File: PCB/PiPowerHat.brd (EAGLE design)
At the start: 65 x 56 mm, 48 parts, among them J3 Display, J4 FAN1, K1 PIN20X2, Q1 NX2301P, U1 EEPROM24, U2 INA219AIDCNRSOIC, U3 TSL2561T, U4 DS18B20, U5 DS1820SOIC, U6 74AC125

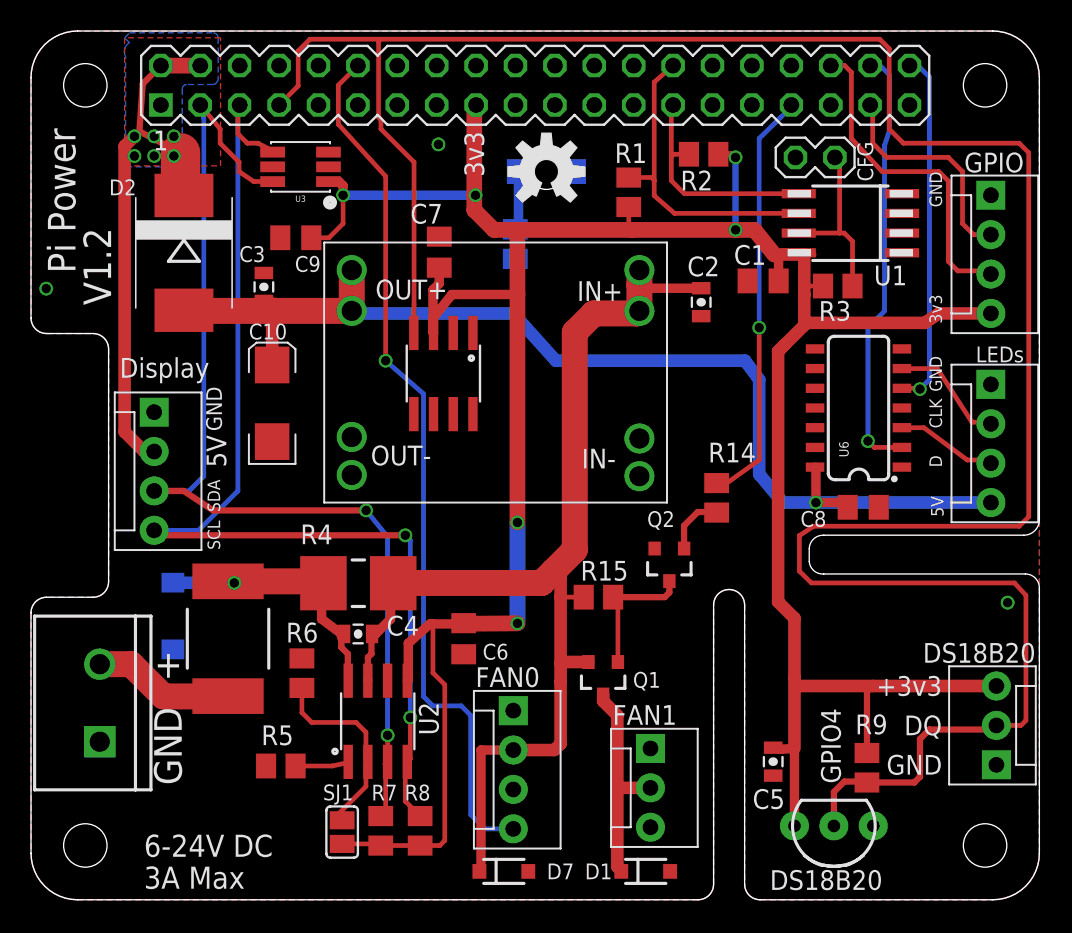
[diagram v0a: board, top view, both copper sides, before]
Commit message: Update to rearrange the board a bit better.
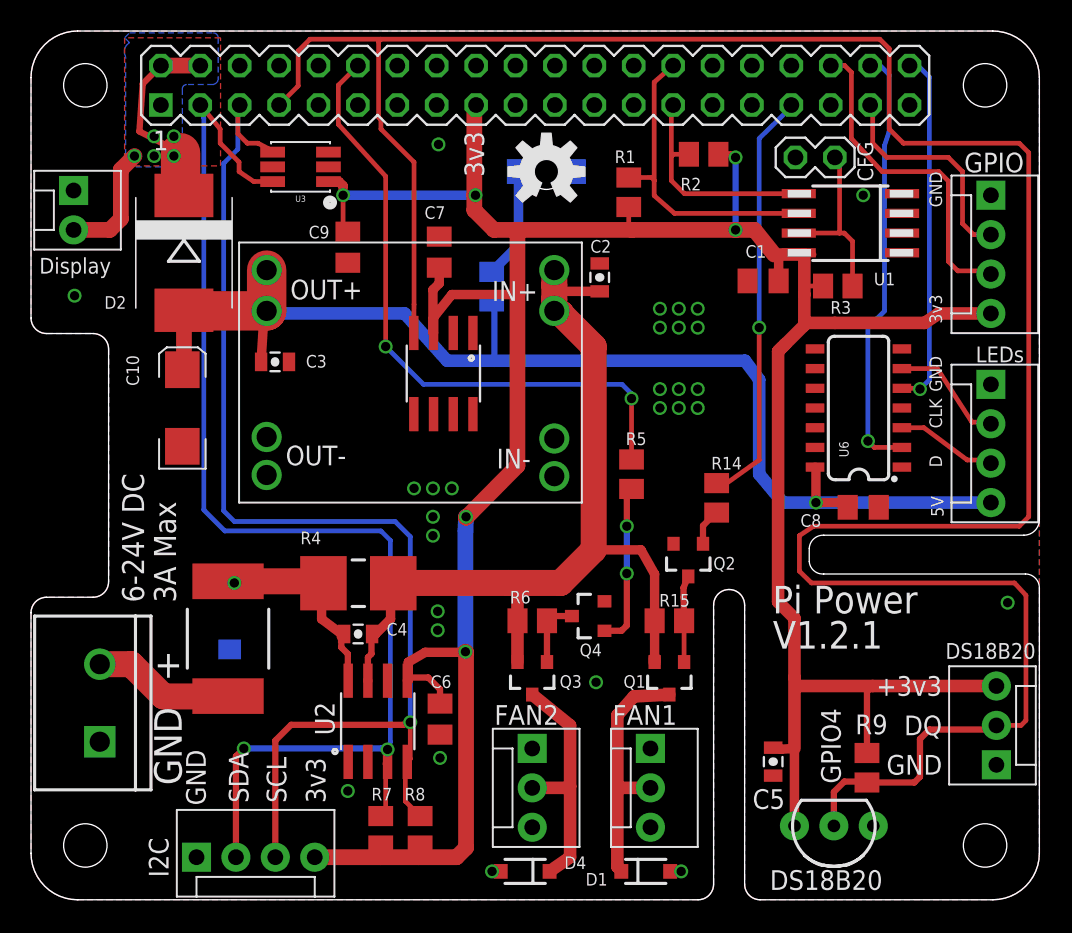
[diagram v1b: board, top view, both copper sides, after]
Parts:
- removed D7: (no value), SparkFun-DiscreteSemi:SOD-123
- removed JP2: FAN0, SparkFun-Connectors:MOLEX-1X4
- removed SJ1: (no value), jumper:SJ
- added D4: (no value), SparkFun-DiscreteSemi:SOD-123
- added J5: I2C, SparkFun-Connectors:MOLEX-1X4
- added JP3: Display, SparkFun-Connectors:MOLEX-1X2
- added Q3: NX2301P, SparkFun-DiscreteSemi:SOT23-3
- added Q4: (no value), SparkFun-DiscreteSemi:SOT23-3
- J3: value Display -> FAN2; device SparkFun-Connectors:MOLEX-1X4 -> SparkFun-Connectors:MOLEX-1X3
- moved J3 32.6 mm to (32.3, 9.75)
- moved R5 29.4 mm to (38.7, 27.4), turned to 90 degrees
- moved R6 15.2 mm to (32.3, 18.0), turned to 180 degrees
- moved C2 6.73 mm to (36.7, 40.1), turned to 270 degrees
- moved C10 5.80 mm to (9.75, 31.7)
- moved U$1 5.49 mm to (13.4, 25.6)
- moved C6 5.40 mm to (26.4, 11.6)
- moved C3 4.89 mm to (15.7, 34.7), turned to 180 degrees
- moved R15 4.82 mm to (41.1, 18.0)
- moved Q1 4.27 mm to (41.1, 14.3)
- moved D6 3.66 mm to (12.8, 18.3)
- moved C9 3.41 mm to (20.4, 42.1), turned to 270 degrees
- moved R12 3.14 mm to (29.7, 39.5)
- moved Q2 1.26 mm to (42.4, 21.9)
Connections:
- removed net FAN0_PWM: JP2.4, K1.12
- removed net N$10: R5.2, U2.1
- removed net N$9: R6.2, SJ1.2, U2.2
- new net FAN2_PWM: K1.12, R5.2
- new net GPIO6: K1.31
- new net N$1: D4.C, J3.2, Q3.3
- new net N$2: Q4.1, R5.1
- new net N$6: Q3.1, Q4.3, R6.1
- net +3V3: now also J5.4; no longer SJ1.1
- net GND: now also D4.A, J5.1, JP3.1, Q4.2, U2.1, U2.2; no longer D7.A, JP2.1, R5.1, R6.1
- net PI_5V: now also JP3.2; no longer J3.2
- net SCL: now also J5.3; no longer J3.4
- net SDA: now also J5.2; no longer J3.3
- net VIN: now also Q3.2, R6.2; no longer D7.C, JP2.2
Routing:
- net FAN0_PWM: track 56.5 -> 0.00 mm, vias 1 -> 0
- net FAN2_PWM: track 0.00 -> 41.2 mm, vias 0 -> 2
- net N$1: track 0.00 -> 15.7 mm
- net PI_5V: track 34.8 -> 20.8 mm, vias 6 -> 5
- net N$9: track 12.9 -> 0.00 mm
- net SDA: track 69.8 -> 81.2 mm
- net N$2: track 0.00 -> 10.5 mm, vias 0 -> 2
- net VIN: track 73.4 -> 63.8 mm
- net SCL: track 71.0 -> 79.0 mm, vias 2 -> 1
- net N$6: track 0.00 -> 5.00 mm
- net N$10: track 4.89 -> 0.00 mm
- net N$5: track 18.3 -> 14.6 mm
- net +3V3: track 198.5 -> 202.0 mm
- net N$4: track 3.81 -> 7.18 mm
- net N$8: track 8.78 -> 5.58 mm
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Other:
- board text added: "FAN2"
- board text added: "I2C"
- board text added: "V1.2.1"
- board text removed: "FAN0"
- board text removed: "V1.2"

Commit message: Removed 3v3/5V logic converter in favour of just a second 3v3 GPIO port.
Added Fan3 which is permenantly connected to the VIn supply to allow it to be used to power a fan or something else whilst still having current monitoring without the current restriction of the p-channel fets.

Slight improvements in routing.
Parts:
- removed C8: 100nF, resistor:C0805K
- removed U6: 74AC125, SparkFun-DigitalIC:SO14
- added D5: (no value), SparkFun-DiscreteSemi:SOD-123
- added D7: (no value), SparkFun-LED:LED-1206
- added J6: FAN3, SparkFun-Connectors:MOLEX-1X3
- added R10: 1k5, resistor:M0805
- JP1: value LEDs -> GPIO2
- JP4: value GPIO -> GPIO1
- moved D3 30.8 mm to (3.35, 39.3), turned to 0 degrees
- moved LOGO1 30.8 mm to (3.35, 39.3)
- moved R12 23.9 mm to (6.27, 34.5), flipped to the top
- moved Q4 9.74 mm to (39.3, 27.4), turned to 180 degrees
- moved R14 6.43 mm to (44.8, 32.3)
- moved D6 6.28 mm to (10.4, 24.1), flipped to the top, turned to 0 degrees
- moved Q2 5.69 mm to (43.9, 27.4)
- moved R6 5.49 mm to (37.8, 17.7), turned to 270 degrees
- moved R5 5.11 mm to (40.2, 32.3)
- moved Q3 2.44 mm to (34.7, 14.3)
- moved U3 0.61 mm to (18.0, 47.2)
- moved C2 0.30 mm to (37.0, 40.1)
- moved C3 0.30 mm to (15.7, 34.4)
- moved D1 0.30 mm to (39.9, 1.83), turned to 180 degrees
- renumbered U$1 to RG1
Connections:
- removed net DOTSTAR_CLOCK: JP1.2, U6.6
- removed net DOTSTAR_DATA: JP1.3, U6.3
- removed net GPIO6: K1.31
- removed net LED_MOSI: K1.38, U6.2
- removed net LED_SCLK: K1.40, U6.5
- new net GPIO11: K1.23, R10.2
- new net GPIO20: JP1.3, K1.38
- new net GPIO21: JP1.2, K1.40
- new net N$9: D7.A, R10.1
- net +3V3: now also JP1.4
- net +5V: no longer C8.1, JP1.4, U6.14
- net GND: now also D5.A, D7.C, J6.1; no longer C8.2, U6.1, U6.10, U6.12, U6.13, U6.4, U6.7, U6.9
- net VIN: now also D5.C, J6.2
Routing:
- net +5V: track 79.9 -> 20.7 mm, vias 1 -> 0
- net GPIO20: track 0.00 -> 32.9 mm
- net LED_MOSI: track 28.0 -> 0.00 mm, vias 1 -> 0
- net GPIO21: track 0.00 -> 27.5 mm
- net LED_SCLK: track 23.1 -> 0.00 mm, vias 1 -> 0
- net VIN: track 63.8 -> 74.6 mm
- net +3V3: track 202.0 -> 211.8 mm, vias 6 -> 5
- net N$6: track 5.00 -> 13.3 mm, vias 0 -> 2
- net DOTSTAR_CLOCK: track 7.66 -> 0.00 mm
- net N$2: track 10.5 -> 2.93 mm, vias 2 -> 0
- net DOTSTAR_DATA: track 6.55 -> 0.00 mm
- net FAN1_PWM: track 27.0 -> 20.6 mm
- net N$8: track 5.58 -> 11.8 mm
- net GPIO11: track 0.00 -> 4.83 mm
- net N$9: track 0.00 -> 3.07 mm
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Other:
- board text added: "26"
- board text added: "5V @ 3A Max"
- board text added: "FAN3"
- board text added: "Fan voltage MUST match input voltage."
- board text added: "GPIO1"
- board text added: "GPIO16"
- board text added: "GPIO2"
- board text added: "GPIO20"
- board text added: "GPIO21"
- board text added: "P1"
- board text removed: "3A Max"
- board text removed: "5V"
- board text removed: "CLK"
- board text removed: "D"
- board text removed: "GPIO"
- board text removed: "LEDs"

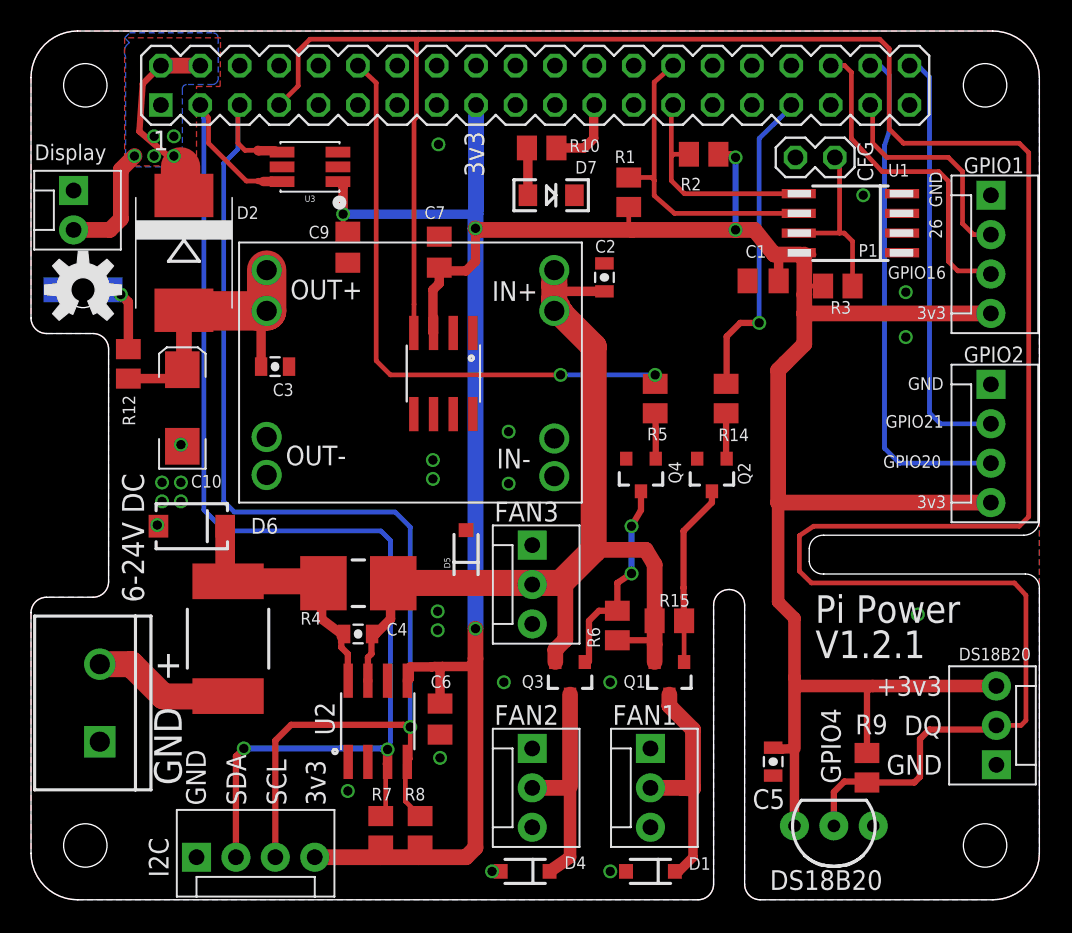
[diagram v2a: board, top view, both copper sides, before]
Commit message: Flipped temperature sensor connector improved silk screen.
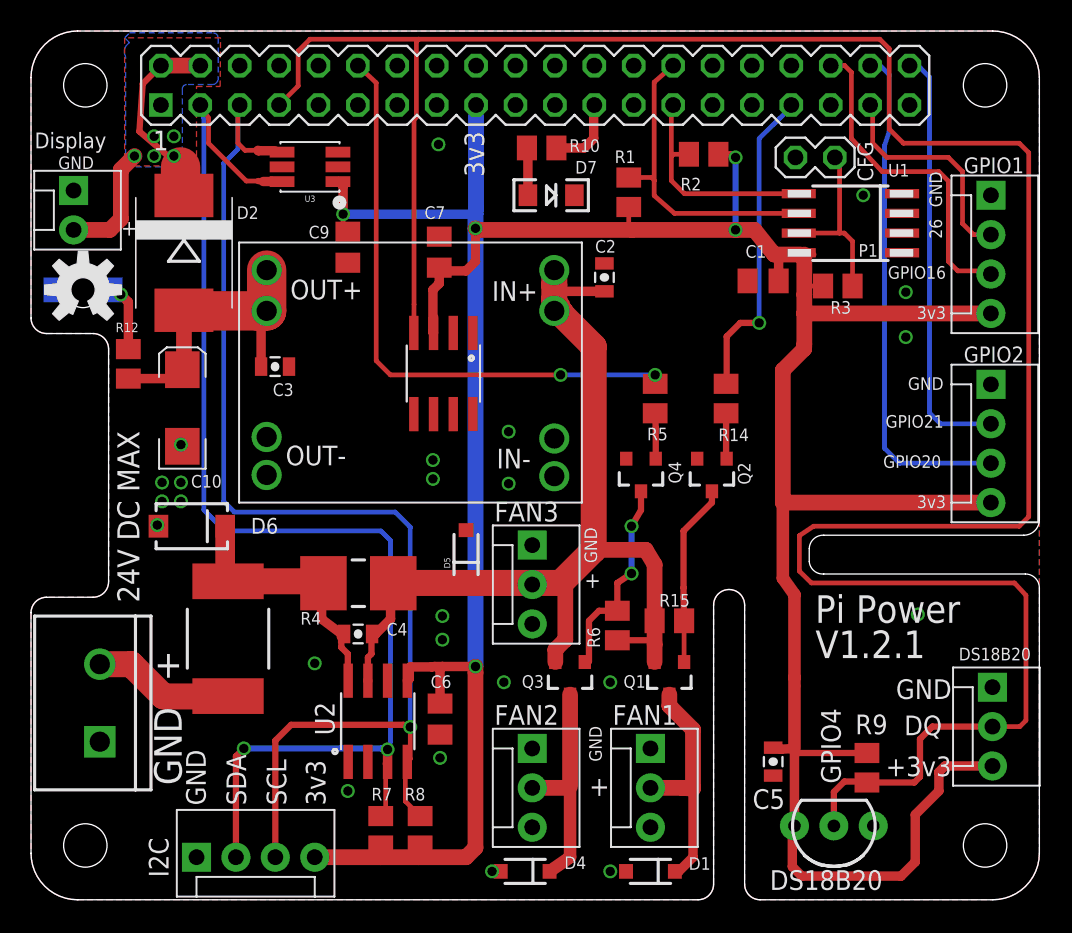
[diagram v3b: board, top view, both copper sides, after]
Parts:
- moved J2 5.01 mm to (62.0, 13.7), turned to 270 degrees
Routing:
- net +3V3: track 211.8 -> 219.9 mm
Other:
- board text added: "24V DC MAX"
- board text removed: "6-24V DC"

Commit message: Updated silk screen. Sent to DirtyPCBs.
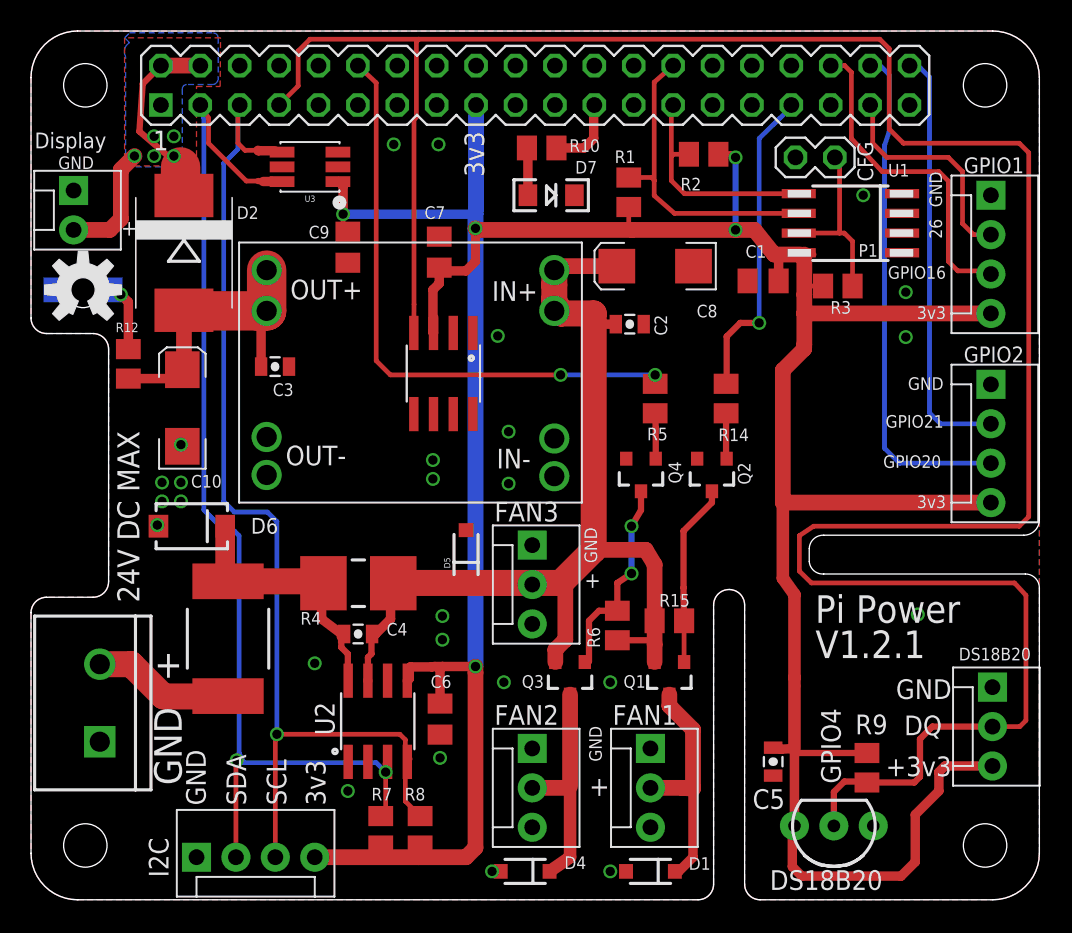
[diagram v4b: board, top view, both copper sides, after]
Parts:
- added C8: 10UF 35V, SparkFun-Capacitors:EIA6032-NOM
- C10: value 10UF -> 100UF 10V
- moved C2 3.43 mm to (38.6, 37.1), turned to 180 degrees
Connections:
- net GND: now also C8.C
- net VIN: now also C8.A
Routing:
- net SCL: track 80.0 -> 71.3 mm
- net SDA: track 82.0 -> 74.5 mm
- net VIN: track 74.6 -> 78.6 mm
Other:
- board text added: "S.Harrison 1 Aug 2017"
- board text removed: "S.Harrison 27 Feb 2017"
